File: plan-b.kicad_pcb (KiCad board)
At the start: 4 copper layers, 55.4 x 42.1 mm, 73 parts, among them J1 HRO_TYPE-C-31-M-14, J2 Battery, J3 rgb, J4 columns, J5 Conn_01x10, J6 rows, J7 sensor, J8 Conn_ARM_SWD_TagConnect_TC203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, J9 Conn_01x05_Pin, J99 Net tie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

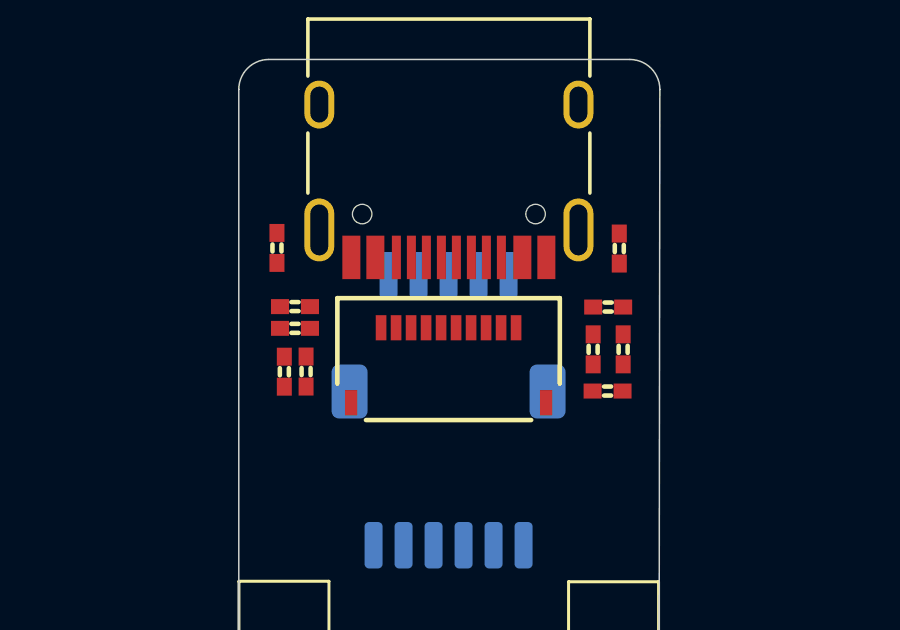
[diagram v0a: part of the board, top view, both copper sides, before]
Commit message: Cleaning up the LCD schematics
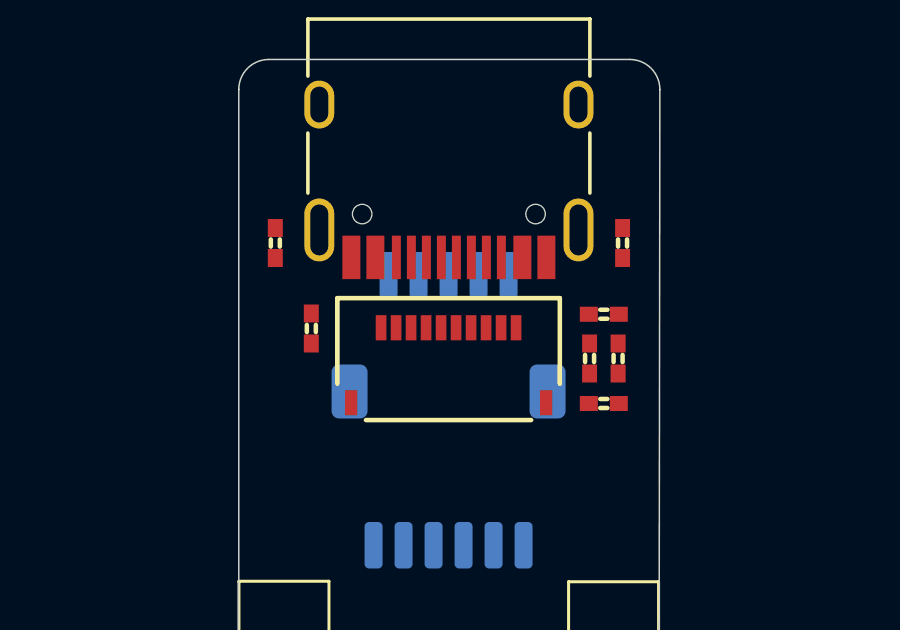
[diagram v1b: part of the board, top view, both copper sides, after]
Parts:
- removed R32, R33, R39: 10k, Library:R_0402_1005
- C37: value 560pF/680pF -> 560pF
- moved C37 0.91 mm to (145.4, 66.6), turned to -90 degrees
- moved C30 0.43 mm to (155.2, 69.1)
- moved FB2 0.35 mm to (155.7, 67.6)
- moved FB1 0.33 mm to (154.7, 67.6)
- moved C38 0.28 mm to (155.2, 66.1)
- moved R21 0.22 mm to (155.8, 63.7)
- moved R22 0.17 mm to (144.2, 63.7)
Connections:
- net CLK renamed LCD CLK
- net CS renamed LCD CS
- net DATA renamed LCD DATA
- J5 pad 4: EXTCOMIN -> GND
- J5 pad 8: EXTMODE -> GND

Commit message: Roughly aligning back and front
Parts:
- moved J2 40.5 mm to (194.0, 93.4)
- moved J3 40.5 mm to (187.6, 93.4)
- moved J4 40.5 mm to (190.5, 75.4)
- moved J6 40.5 mm to (190.5, 66.4)
- moved J7 40.5 mm to (190.5, 84.4)
- moved R16 7.58 mm to (194.9, 77.8), turned to 90 degrees
- moved R15 6.48 mm to (195.8, 77.8), turned to 90 degrees
- moved R14 5.46 mm to (196.7, 77.8), turned to 90 degrees
- moved R11 4.56 mm to (197.6, 77.8), turned to 90 degrees
- moved SW1 4.09 mm to (184.1, 89.4)
- moved SW2 4.09 mm to (183.8, 96.6)
- moved R_DIV1 3.84 mm to (192.7, 92.3)
- moved R_DIV2 3.84 mm to (192.0, 92.3)
- moved U4 3.84 mm to (190.5, 87.8)
- moved C44 3.84 mm to (188.2, 87.6)
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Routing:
- net VDD: track 48.4 -> 15.8 mm
- net VSYS: track 27.0 -> 13.3 mm, vias 3 -> 1
- net Net-(U1-DEC4): track 16.3 -> 6.68 mm
- net unconnected-(U1-P0.26-PadG1): track 7.75 -> 0.01 mm
- net unconnected-(U1-P0.04/AIN2-PadJ1): track 7.66 -> 0.01 mm
- net unconnected-(U1-P0.06-PadL1): track 7.58 -> 0.00 mm
- net unconnected-(U1-P0.08-PadN1): track 7.49 -> 0.00 mm
- net unconnected-(U1-P1.09-PadR1): track 7.41 -> 0.00 mm
- net unconnected-(U1-P0.12-PadU1): track 7.32 -> 0.00 mm
- net unconnected-(U1-P1.10-PadA20): track 6.50 -> 0.00 mm
- net unconnected-(U1-P1.13-PadA16): track 6.47 -> 0.01 mm
- net unconnected-(U1-P1.15-PadA14): track 6.38 -> 0.00 mm
- net unconnected-(U1-P0.13-PadAD8): track 6.32 -> 0.00 mm
- net unconnected-(U1-P0.02/AIN0-PadA12): track 6.30 -> 0.00 mm
- net unconnected-(U1-P0.31/AIN7-PadA8): track 6.27 -> 0.00 mm
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
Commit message: Optimising the RF side
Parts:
- R_ICHG1: renamed from R_ICHG; value 4k7 -> 4.7k
- SW2 (x2): footprint Button_Switch_SMD:SW_SPST_B3U-3000P -> Button_Switch_SMD:SW_SPST_B3U-3000P-B
- moved C22 19.2 mm to (210.4, 60.7)
- moved C23 19.2 mm to (209.3, 63.0)
- moved C24 19.2 mm to (210.5, 63.4)
- moved C25 19.2 mm to (214.0, 65.0)
- moved J99 19.2 mm to (215.9, 64.2)
- moved L5 19.2 mm to (214.5, 66.1)
- moved R3 19.2 mm to (210.6, 58.4)
- moved R_ICHG1 19.2 mm to (212.6, 58.4)
- moved U2 19.2 mm to (213.8, 61.7)
- moved C26 19.2 mm to (216.3, 65.5)
- moved LD2 18.7 mm to (215.2, 58.5)
- moved J8 13.6 mm to (184.1, 78.1)
- moved X1 2.18 mm to (184.9, 83.4), turned to -90 degrees
- moved C1 2.17 mm to (183.5, 83.3), turned to -90 degrees
- moved C11 1.73 mm to (184.8, 81.7)
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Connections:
- AE1 pad 2: (no net) -> GND
- X1 pad 2: unconnected-(X1-GND-Pad2) -> GND
- X1 pad 4: unconnected-(X1-GND-Pad4) -> GND
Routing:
- net D+: track 12.1 -> 3.41 mm
- net D-: track 11.7 -> 3.69 mm
- net GND: track 13.7 -> 20.9 mm, vias 24 -> 22
- net VSYS: track 13.3 -> 8.34 mm, vias 1 -> 2
- net VBUS: track 11.7 -> 7.32 mm, vias 0 -> 1
- net Net-(U1-XC1): track 5.76 -> 3.67 mm
- net Net-(LD2-C): track 1.58 -> 0.00 mm
- net /MCU/RF: track 8.12 -> 6.63 mm
- net Net-(U1-XC2): track 4.34 -> 3.02 mm
- net SWDIO: track 2.11 -> 0.85 mm, vias 0 -> 1
- net Net-(U1-DEC3): track 3.05 -> 1.92 mm
- net Net-(U1-DEC4): track 6.68 -> 5.60 mm
- net SWCLK: track 2.58 -> 1.61 mm, vias 0 -> 1
- net unconnected-(U2-VTERM-Pad9): track 0.77 -> 0.00 mm, vias 1 -> 0
- net VDD: track 15.8 -> 15.1 mm
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
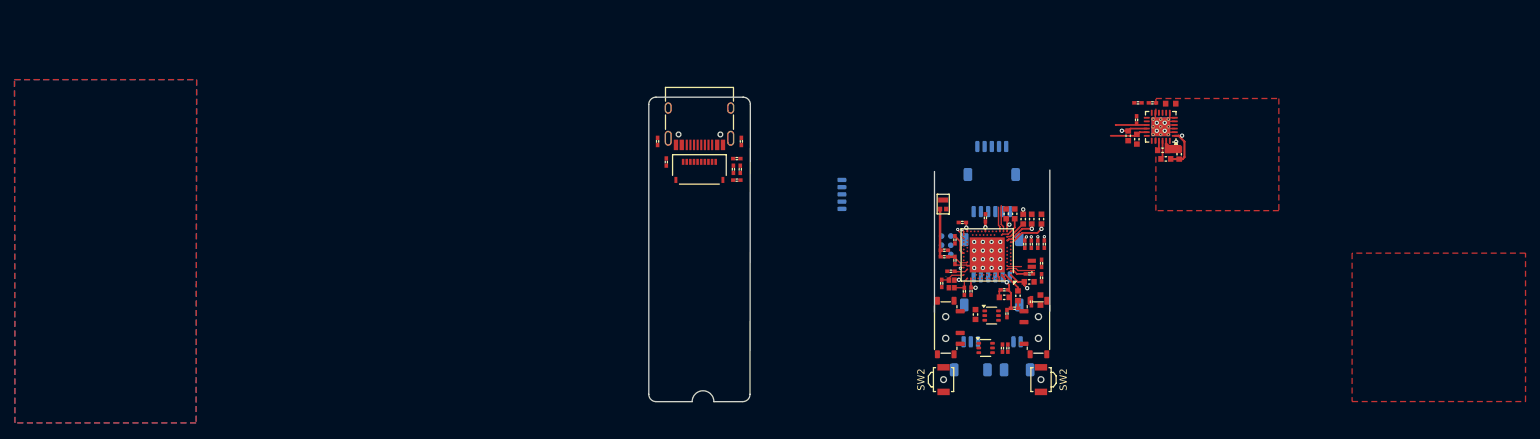
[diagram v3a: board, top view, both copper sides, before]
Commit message: Re-working the PCB cutouts to 16x42mm dimensions and realigning switches and connectors at the back
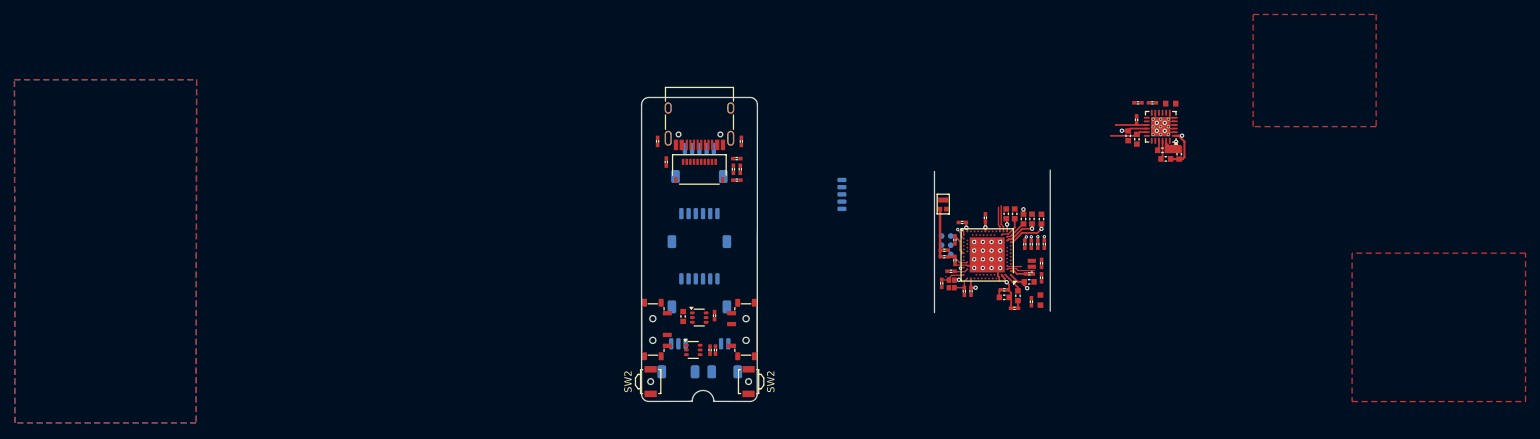
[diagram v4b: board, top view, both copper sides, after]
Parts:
- moved SW1 40.5 mm to (143.6, 89.7)
- moved SW2 40.5 mm to (143.3, 96.9)
- moved C44 40.4 mm to (147.7, 87.9)
- moved J2 40.4 mm to (153.5, 93.7)
- moved J3 40.4 mm to (147.1, 93.7)
- moved J4 40.4 mm to (150.0, 75.7)
- moved J6 40.4 mm to (150.0, 66.7)
- moved J7 40.4 mm to (150.0, 84.7)
- moved R8 40.4 mm to (152.1, 87.8)
- moved R_DIV1 40.4 mm to (152.2, 92.6)
- moved R_DIV2 40.4 mm to (151.5, 92.6)
- moved SW1 40.4 mm to (156.4, 89.7)
- moved SW2 40.4 mm to (156.8, 96.9)
- moved U3 40.4 mm to (149.2, 92.5)
- moved U4 40.4 mm to (150.0, 88.1)
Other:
- board size 55.4 x 42.1 mm -> 56.5 x 42 mm

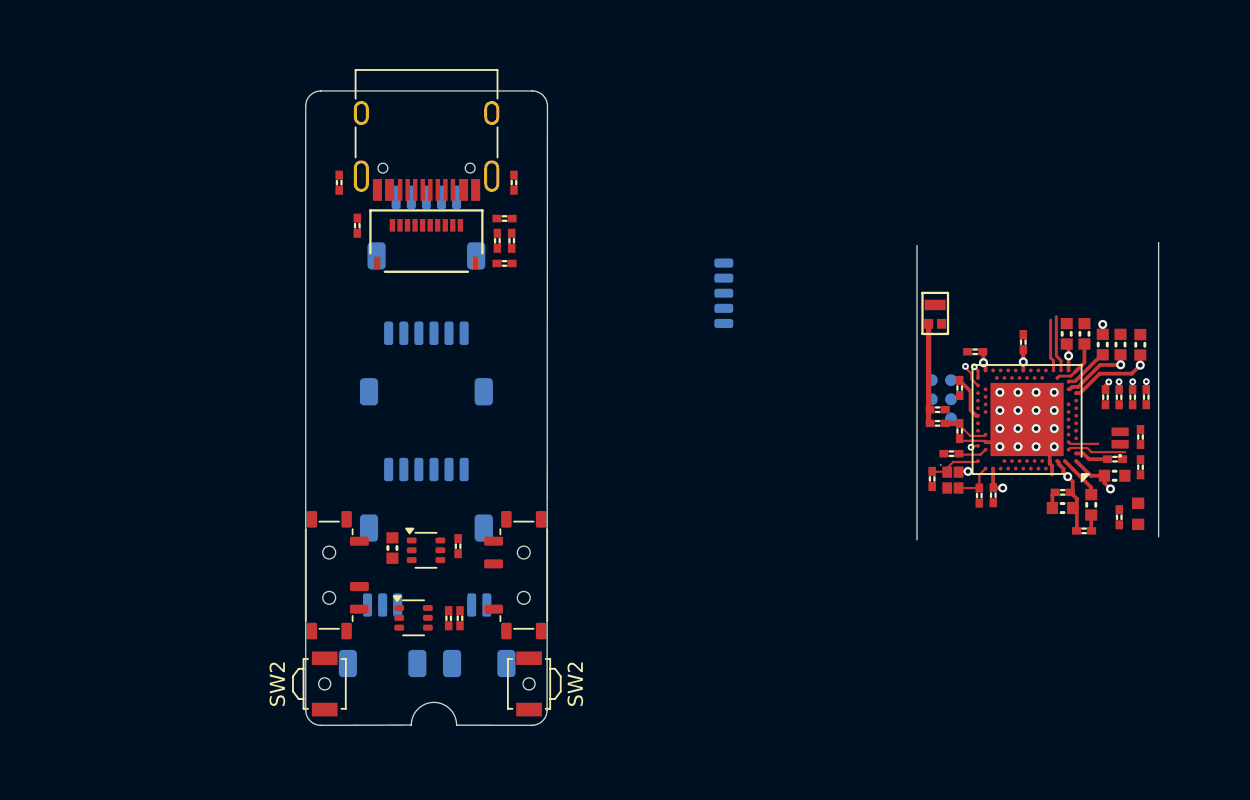
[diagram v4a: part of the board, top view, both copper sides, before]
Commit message: Trying the 18x42mm form factor
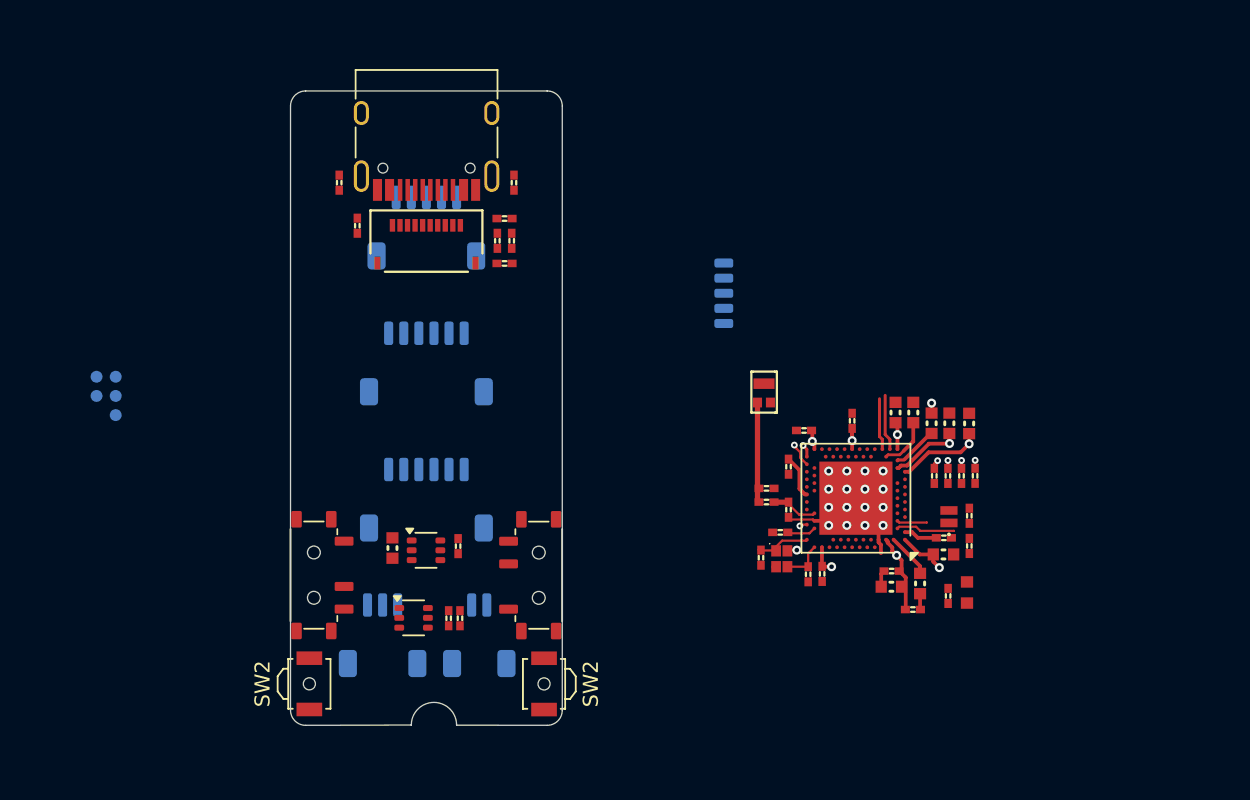
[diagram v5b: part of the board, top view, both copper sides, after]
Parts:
- moved J8 55.3 mm to (128.8, 77.8)
- moved C1 12.5 mm to (172.2, 88.6)
- moved C11 12.5 mm to (173.4, 86.9)
- moved C12 12.5 mm to (176.2, 89.6)
- moved C20 12.5 mm to (182.3, 79.0)
- moved C21 12.5 mm to (181.1, 79.0)
- moved C3 12.5 mm to (174.0, 85.4)
- moved C4 12.5 mm to (172.5, 84.0)
- moved C5 12.5 mm to (184.3, 87.3)
- moved C7 12.5 mm to (178.2, 79.5)
- moved C8 12.5 mm to (175.0, 80.1)
- moved L1 12.5 mm to (172.5, 84.9)
- moved L3 12.5 mm to (182.2, 92.0)
- moved LD3 12.5 mm to (185.8, 90.9)
- moved R14 12.5 mm to (185.4, 83.1)
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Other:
- board size 56.5 x 42 mm -> 18 x 42 mm

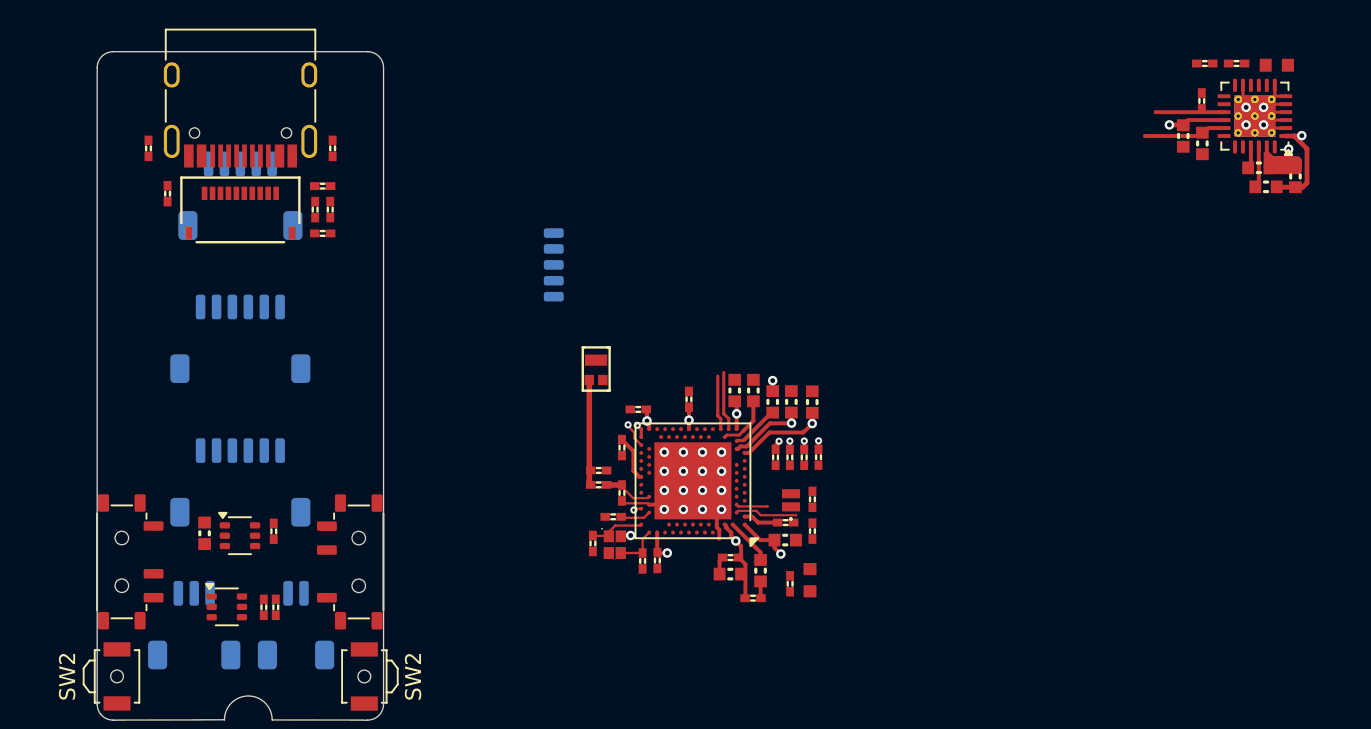
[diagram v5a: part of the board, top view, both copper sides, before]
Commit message: Moving the main block in place
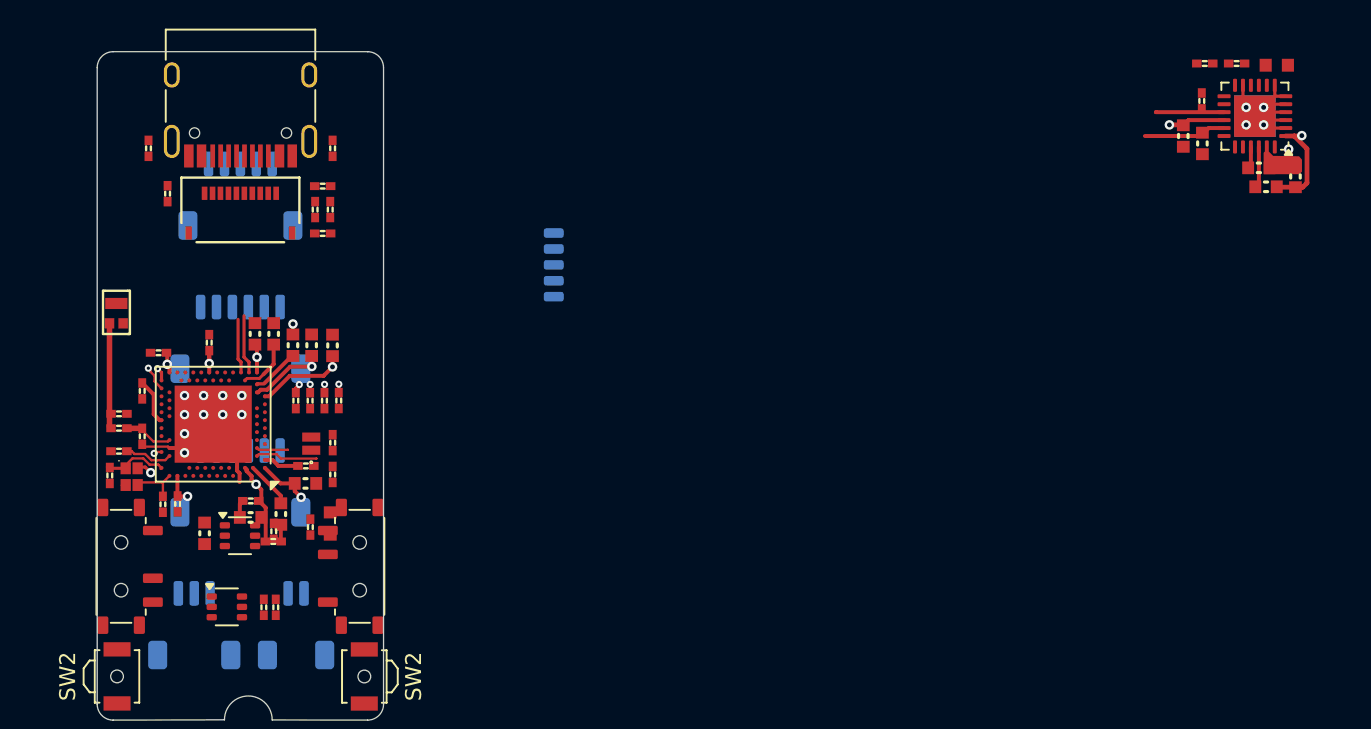
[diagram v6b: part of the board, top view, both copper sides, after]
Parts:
- moved C11 31.3 mm to (142.4, 82.8)
- moved C1 30.7 mm to (141.8, 84.3)
- moved X1 30.7 mm to (143.2, 84.4)
- moved AE1 30.4 mm to (142.3, 74.1)
- moved C12 30.4 mm to (146.1, 86.1)
- moved C14 30.4 mm to (154.1, 84.8)
- moved C15 30.4 mm to (150.6, 86.9)
- moved C17 30.4 mm to (155.8, 84.2)
- moved C18 30.4 mm to (155.8, 82.2)
- moved C2 30.4 mm to (145.1, 86.1)
- moved C20 30.4 mm to (152.1, 75.4)
- moved C21 30.4 mm to (150.9, 75.4)
- moved C4 30.4 mm to (142.4, 80.4)
- moved C5 30.4 mm to (154.1, 83.7)
- moved L1 30.4 mm to (142.4, 81.3)
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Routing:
- net Net-(U1-DEC3): track 1.92 -> 3.02 mm
- net GND: track 20.9 -> 21.4 mm, vias 22 -> 16
